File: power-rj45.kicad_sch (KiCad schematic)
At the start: 29 parts, among them J101 2x05_Horizontal, J102 NE8FAH, J103 JAE_DX07S016JA3, J104 2x05_Horizontal, J105 NE8FAH, J501 WAGO-2065, J502 WAGO-2065

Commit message: Update to Kicad 8
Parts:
- renumbered C205 to C102, J501 to J106, J502 to J107, J501 to J108, J502 to J109, TVS201 to TVS101

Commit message: Update icons
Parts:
- removed ICON101, ICON104: Minus, V2_Artwork:Minus_Small, symbol V2_Artwork:Minus
- added ICON110, ICON111: Arrow_Out, V2_Artwork:Arrow_Out, symbol V2_Artwork:Arrow_Out
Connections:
- net VBUS: now reaches J103.V (VBUS)
- no-connect marks 7 -> 6

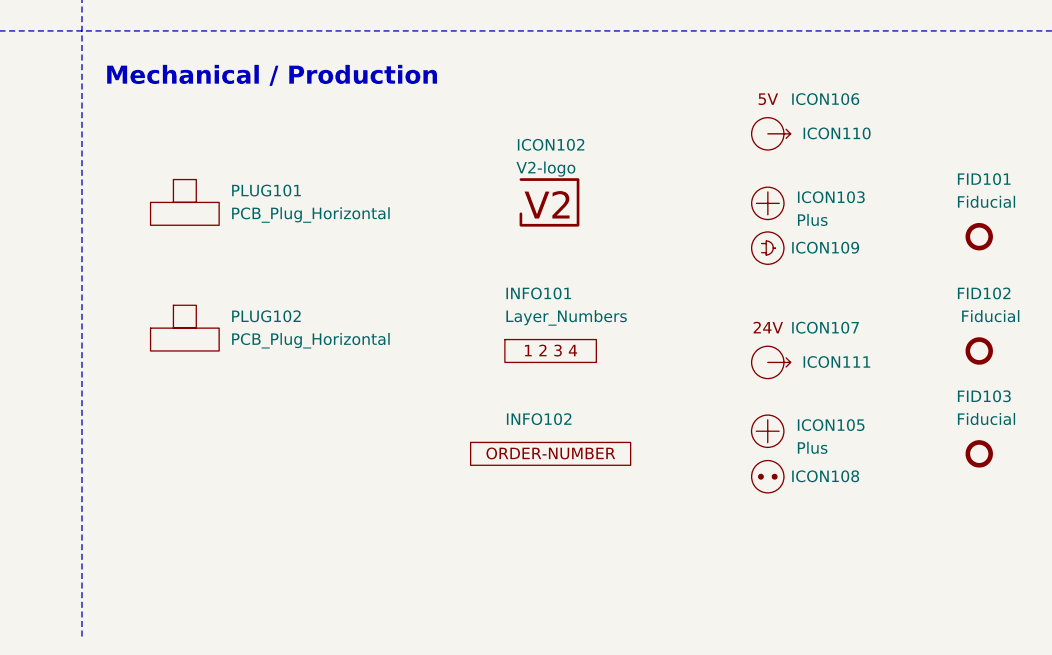
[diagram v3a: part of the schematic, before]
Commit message: Replace icons
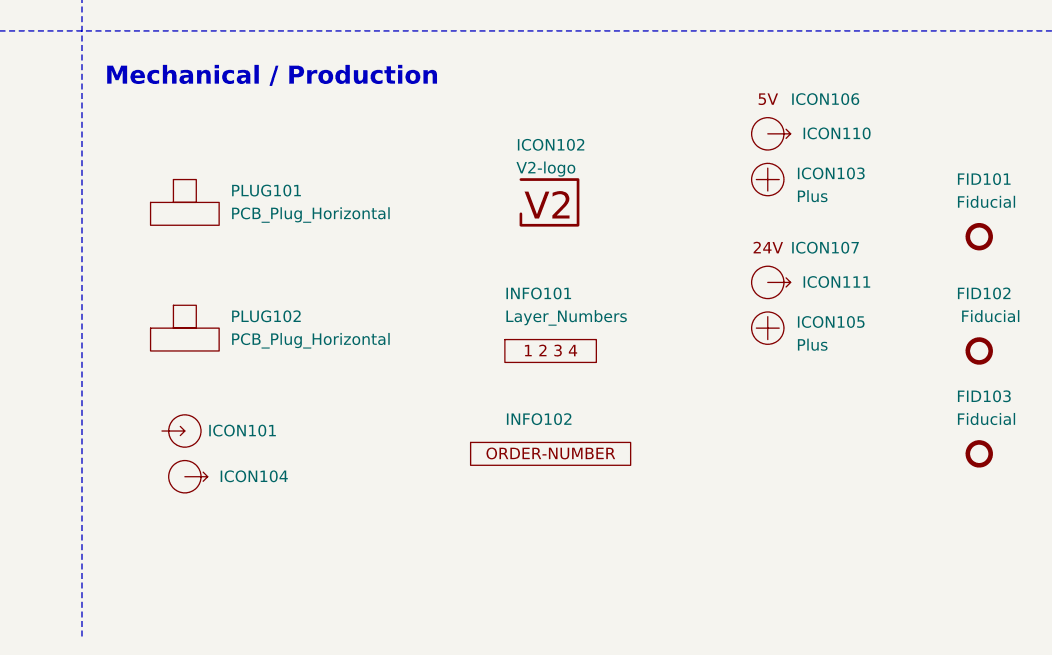
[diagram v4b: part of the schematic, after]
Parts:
- removed ICON108: Socket, V2_Artwork:Socket_Small, symbol V2_Artwork:Socket
- removed ICON109: Plug, V2_Artwork:Plug_Small, symbol V2_Artwork:Plug
- added ICON101: Arrow_In, V2_Artwork:Arrow_In, symbol V2_Artwork:Arrow_In
- added ICON104: Arrow_Out, V2_Artwork:Arrow_Out, symbol V2_Artwork:Arrow_Out
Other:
- moved on the sheet: ICON103, ICON105, ICON107, ICON111
